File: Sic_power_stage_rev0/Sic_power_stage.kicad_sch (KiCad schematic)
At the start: 39 parts, among them J1 20021321-00006C4LF, J2 20021321-00006C4LF, J3 20021321-00006C4LF, J4 20021321-00006C4LF, J5 20021321-00006C4LF, J6 20021321-00006C4LF, J7 20021321-00006C4LF, J8 20021321-00006C4LF

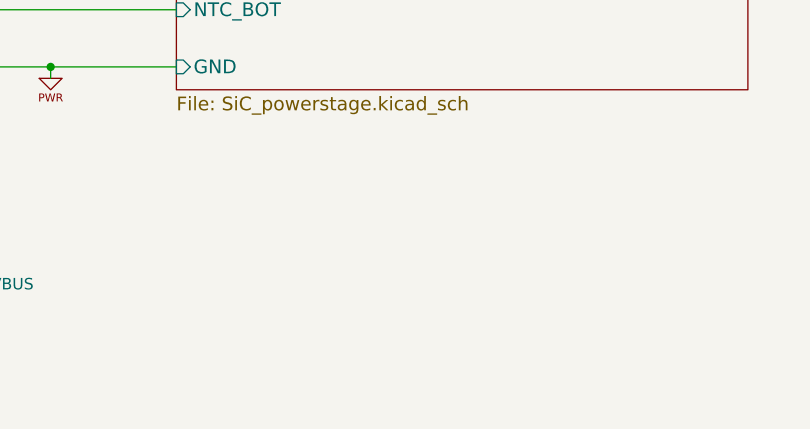
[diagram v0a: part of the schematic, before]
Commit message: WIP: define custom rules, change inner layer PWRGND , VBUS
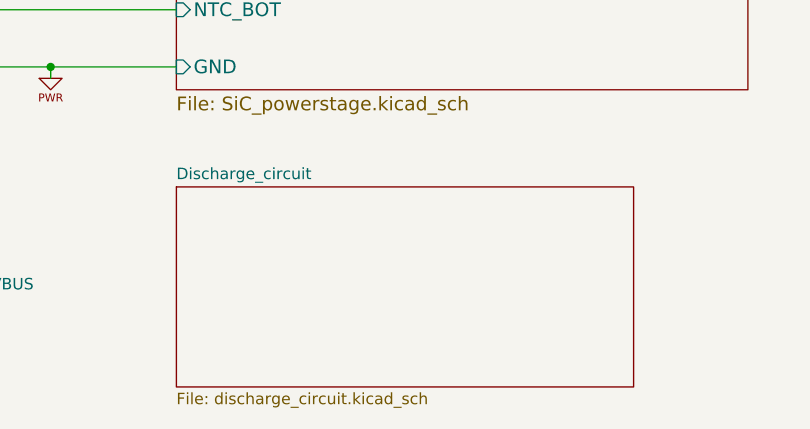
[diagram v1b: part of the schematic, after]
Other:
- added sheet Discharge_circuit (discharge_circuit.kicad_sch)
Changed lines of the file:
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@@
+	)
+	(sheet
+		(at 119.38 170.815)
+		(size 50.8 22.225)
+		(fields_autoplaced yes)
+		(stroke
+			(width 0.1524)
+			(type solid)
+		)
+		(fill
+			(color 0 0 0 0.0000)
+		)
+		(property "Sheetname" "Discharge_circuit"
+			(at 119.38 170.1034 0)
+			(effects
+				(font
+					(size 1.27 1.27)
+				)
+				(justify left bottom)
+			)
+		)
+		(property "Sheetfile" "discharge_circuit.kicad_sch"
+			(at 119.38 193.6246 0)
+			(effects
+				(font
+					(size 1.27 1.27)
+				)
+				(justify left top)
+			)
+		)
+		(instances
+			(project "Sic_power_stage"
+				(path "/40c6bde6-dca0-40b2-8abd-1f20772cb34b"
+					(page "5")
+				)
+			)
+		)
 	)
 	(sheet

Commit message: Increase clearance between mosfets, Add alternating film capacitor
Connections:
- net nc: now reaches J2.1
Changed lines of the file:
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@@
 	)
 	(no_connect
-		(at 100.33 55.88)
+		(at 99.06 58.42)
 	)
 	(no_connect
@@
 	(wire
 		(pts
+			(xy 99.06 55.88) (xy 99.06 58.42)
+		)
+		(stroke
+			(width 0)
+			(type default)
+		)
+	)
+	(wire
+		(pts
 			(xy 110.49 132.08) (xy 119.38 132.08)
 		)
@@
 			(type default)
 			(color 0 0 255 1)
+		)
+	)
+	(wire
+		(pts
+			(xy 100.33 55.88) (xy 99.06 55.88)
+		)
+		(stroke
+			(width 0)
+			(type default)
 		)
 	)
@@
 			)
 			(justify left bottom)
+		)
+	)
+	(label "nc"
+		(at 99.06 55.88 0)
+		(fields_autoplaced yes)
+		(effects
+			(font
+				(size 1.27 1.27)
+			)
+			(justify left bottom)

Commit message: Define Ceralink capacitor value and qty
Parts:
- renumbered J7 to J1, J8 to J2, J1 to J3, J2 to J4, J3 to J5, J4 to J6, J5 to J7, J6 to J8, R40 to R1, R41 to R2, R42 to R3, STANDOFF16 to STANDOFF1, STANDOFF5 to STANDOFF10, STANDOFF6 to STANDOFF11, STANDOFF7 to STANDOFF12, STANDOFF8 to STANDOFF13, STANDOFF9 to STANDOFF14, STANDOFF10 to STANDOFF15, STANDOFF11 to STANDOFF16, STANDOFF12 to STANDOFF17, STANDOFF13 to STANDOFF18, STANDOFF14 to STANDOFF19, STANDOFF17 to STANDOFF2, STANDOFF15 to STANDOFF20, STANDOFF18 to STANDOFF3, STANDOFF19 to STANDOFF4, STANDOFF20 to STANDOFF5, STANDOFF1 to STANDOFF6, STANDOFF2 to STANDOFF7, STANDOFF3 to STANDOFF8, STANDOFF4 to STANDOFF9

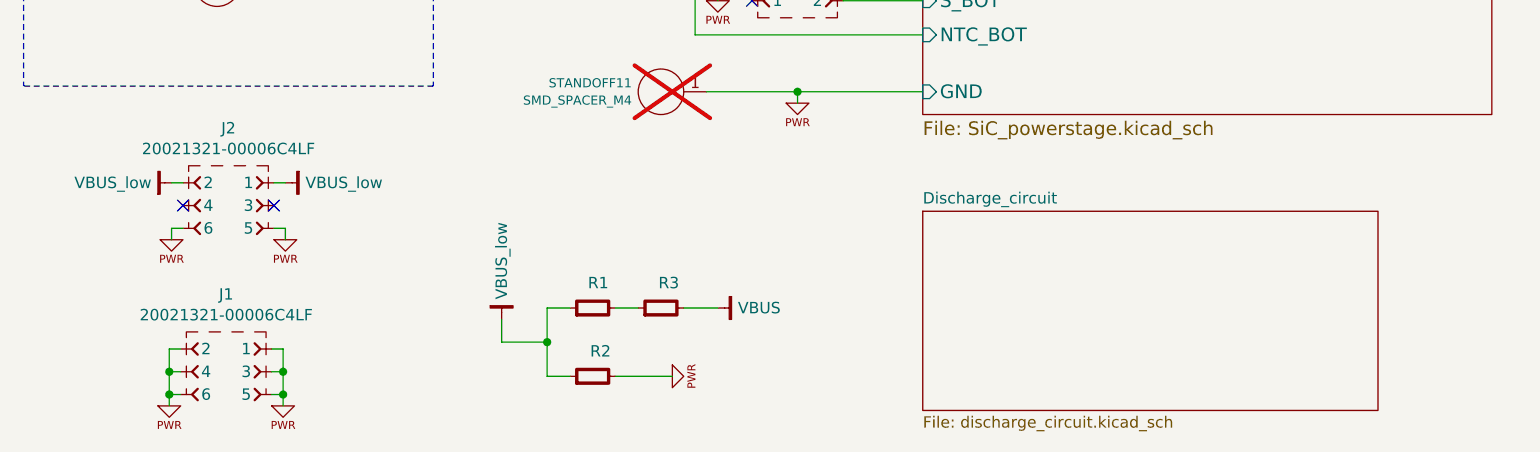
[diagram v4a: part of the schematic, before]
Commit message: Add changes
 - Add DC-LINK capacitor discharge circuit.
 - VBUS resistive divider.
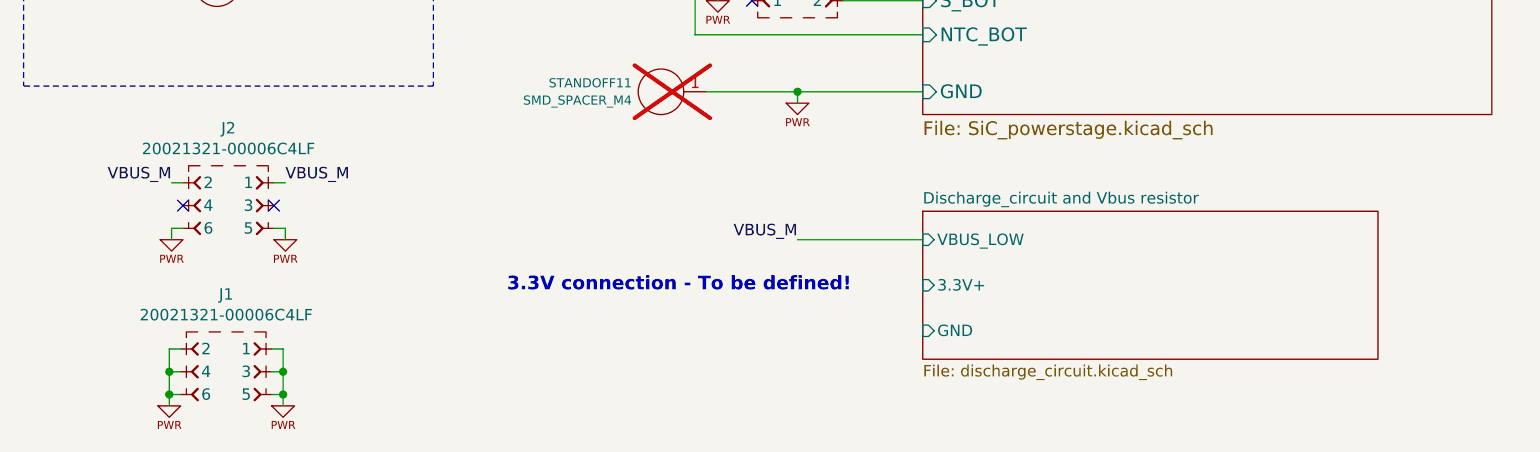
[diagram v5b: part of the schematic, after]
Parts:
- removed R1, R2, R3: R-1206, IPC7351-Nominal:RESC3216X60, symbol pasv-res:R-1206
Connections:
- net VBUS_low renamed VBUS_M
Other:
- sheet Discharge_circuit renamed Discharge_circuit and Vbus resistor
- sheet Discharge_circuit and Vbus resistor ports: added 3.3V+, GND, VBUS_LOW; removed none
- note added: "3.3V connection - To be defined!"

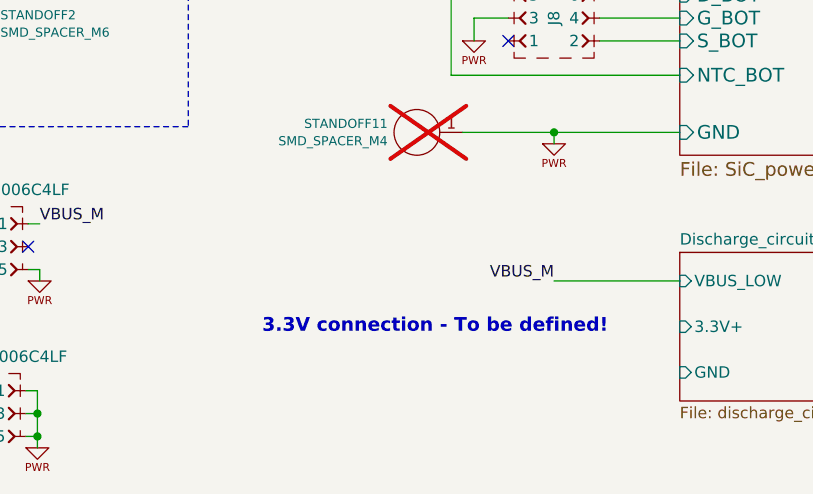
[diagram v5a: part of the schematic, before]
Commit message: SiC: define routing for leg C
Signed-off-by: Ayarde Christian <cayarde@paltatech.com>
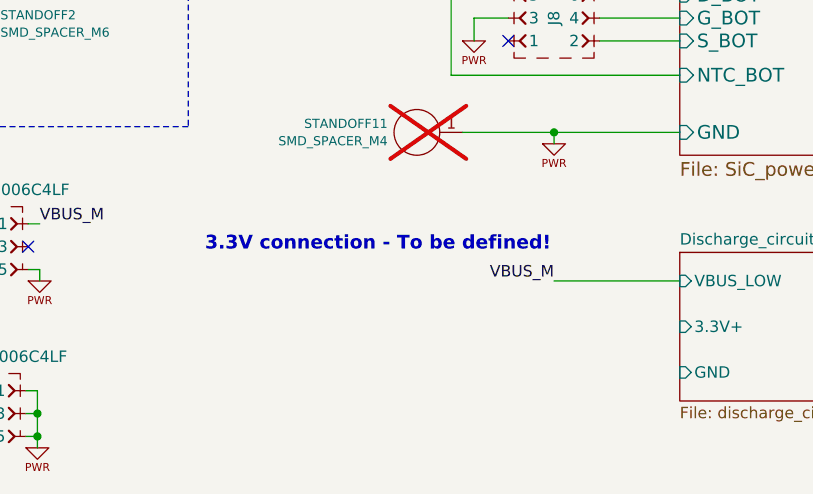
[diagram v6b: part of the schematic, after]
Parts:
- J1, J2, J3, J4, J5, J6, J7, J8: footprint conn-fci:CONN-20021321-00006C4LF -> conn-fci:CONN-20021321-00006C4LF-no-hole
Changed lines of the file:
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@@
 	(text "3.3V connection - To be defined!"
 		(exclude_from_sim no)
-		(at 92.202 179.07 0)
+		(at 85.852 169.926 0)
 		(effects
 			(font
@@
 			)
 		)
-		(property "Footprint" "conn-fci:CONN-20021321-00006C4LF"
+		(property "Footprint" "conn-fci:CONN-20021321-00006C4LF-no-hole"
 			(at 105.41 127 0)
 			(effects
@@
 			)
 		)
-		(property "Footprint" "conn-fci:CONN-20021321-00006C4LF"
+		(property "Footprint" "conn-fci:CONN-20021321-00006C4LF-no-hole"
 			(at 41.656 186.182 0)
 			(effects
@@
 			)
 		)
-		(property "Footprint" "conn-fci:CONN-20021321-00006C4LF"
+		(property "Footprint" "conn-fci:CONN-20021321-00006C4LF-no-hole"
 			(at 41.91 167.64 0)
 			(effects
@@
 			)
 		)
-		(property "Footprint" "conn-fci:CONN-20021321-00006C4LF"
+		(property "Footprint" "conn-fci:CONN-20021321-00006C4LF-no-hole"
 			(at 105.41 55.88 0)
 			(effects
@@
 			)
 		)
-		(property "Footprint" "conn-fci:CONN-20021321-00006C4LF"
+		(property "Footprint" "conn-fci:CONN-20021321-00006C4LF-no-hole"
 			(at 105.41 101.6 0)
 			(effects
@@
 			)
 		)
-		(property "Footprint" "conn-fci:CONN-20021321-00006C4LF"
+		(property "Footprint" "conn-fci:CONN-20021321-00006C4LF-no-hole"
 			(at 105.41 35.56 0)
 			(effects
@@
 			)
 		)
-		(property "Footprint" "conn-fci:CONN-20021321-00006C4LF"
+		(property "Footprint" "conn-fci:CONN-20021321-00006C4LF-no-hole"
 			(at 105.41 81.28 0)
 			(effects
@@
 			)
 		)
-		(property "Footprint" "conn-fci:CONN-20021321-00006C4LF"
+		(property "Footprint" "conn-fci:CONN-20021321-00006C4LF-no-hole"
 			(at 105.41 147.32 0)
 			(effects

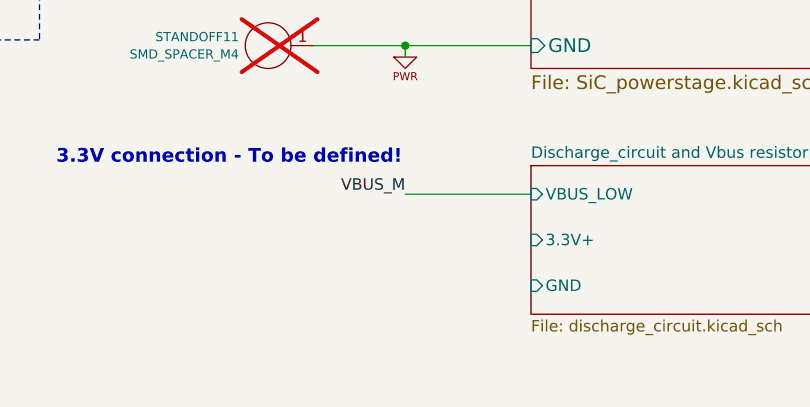
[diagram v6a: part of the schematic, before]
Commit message: SiC: Change DC-LINK MLCC capacitor
 - Originally, the estimation about the ceramic capacitor value was 0.25uF. This is for CERALINK capacitor as the DC-BIAS
   affects its capacitance just 1% for 400V. Now a MLCC was chosen, and the DC-BIAS is into account for this application
   would be great to test with both capacitors and check the bahaviour between them.

Signed-off-by: Ayarde Christian <cayarde@paltatech.com>
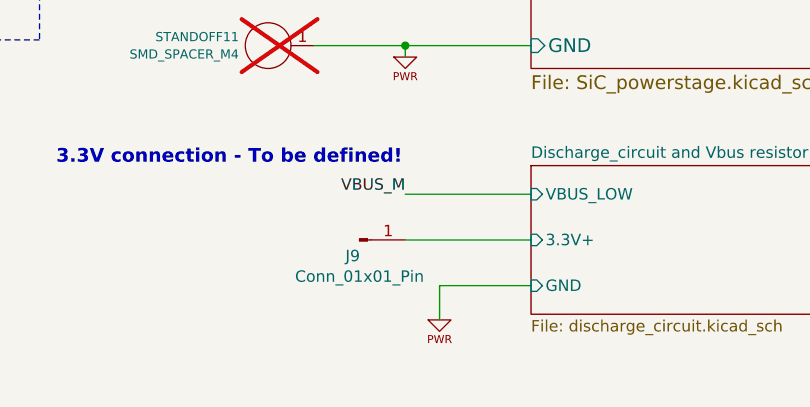
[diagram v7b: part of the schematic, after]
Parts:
- added J9: Conn_01x01_Pin, Connector_PinHeader_1.00mm:PinHeader_1x01_P1.00mm_Vertical, symbol Connector:Conn_01x01_Pin
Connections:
- net Discharge_circuit and Vbus resistor/3.3V+: now also J9.1 (Pin_1)
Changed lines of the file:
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@@
 	(wire
 		(pts
+			(xy 109.22 187.96) (xy 109.22 184.15)
+		)
+		(stroke
+			(width 0)
+			(type default)
+		)
+	)
+	(wire
+		(pts
 			(xy 36.576 188.722) (xy 35.306 188.722)
 		)
@@
 	(wire
 		(pts
+			(xy 109.22 184.15) (xy 119.38 184.15)
+		)
+		(stroke
+			(width 0)
+			(type default)
+		)
+	)
+	(wire
+		(pts
 			(xy 35.306 192.532) (xy 35.306 191.262)
 		)
@@
 	(wire
 		(pts
+			(xy 105.41 179.07) (xy 119.38 179.07)
+		)
+		(stroke
+			(width 0)
+			(type default)
+		)
+	)
+	(wire
+		(pts
 			(xy 95.25 157.48) (xy 105.41 157.48)
 		)
@@
 	)
 	(symbol
+		(lib_id "power1:PWRGND")
+		(at 109.22 187.96 0)
+		(unit 1)
+		(exclude_from_sim no)
+		(in_bom yes)
+		(on_board yes)
+		(dnp no)
+		(property "Reference" "#PWR010"
+			(at 109.22 187.96 0)
+			(effects
+				(font
+					(size 0.762 0.762)
+				)
+				(hide yes)
+			)
+		)
+		(property "Value" "PWRGND"
+			(at 109.22 189.738 0)
+			(effects
+				(font
+					(size 0.762 0.762)
+				)
+				(hide yes)
+			)
+		)
+		(property "Footprint" ""
+			(at 109.22 187.96 0)
+			(effects
+				(font
+					(size 1.524 1.524)
+				)
+			)
+		)
+		(property "Datasheet" ""
+			(at 109.22 187.96 0)
+			(effects
+				(font
+					(size 1.524 1.524)
+				)
+			)
+		)
+		(property "Description" ""
+			(at 109.22 187.96 0)
+			(effects
+				(font
+					(size 1.27 1.27)
+				)
+				(hide yes)
+			)
+		)
+		(pin "1"
+		)
+		(instances
+			(project "Sic_power_stage"
+				(path "/40c6bde6-dca0-40b2-8abd-1f20772cb34b"
+					(reference "#PWR010")
+					(unit 1)
+				)
+			)
+		)
+	)
+	(symbol
 		(lib_id "conn-100mil:CONN-100MIL-F-2x3")
 		(at 105.41 35.56 0)
@@
 					(unit 1)
 				)
+			)
+		)
+	)
+	(symbol
+		(lib_id "Connector:Conn_01x01_Pin")
+		(at 100.33 179.07 0)
+		(unit 1)
+		(exclude_from_sim no)
+		(in_bom yes)
+		(on_board yes)
+		(dnp no)
+		(property "Reference" "J9"
+			(at 99.568 180.848 0)
+			(effects
+				(font
+					(size 1.27 1.27)
+				)
+			)
+		)
+		(property "Value" "Conn_01x01_Pin"
+			(at 100.33 183.134 0)
+			(effects
+				(font
+					(size 1.27 1.27)
+				)
+			)
+		)
+		(property "Footprint" "Connector_PinHeader_1.00mm:PinHeader_1x01_P1.00mm_Vertical"
+			(at 100.33 179.07 0)
+			(effects
+				(font
+					(size 1.27 1.27)
+				)
+				(hide yes)
+			)
+		)
+		(property "Datasheet" "~"
+			(at 100.33 179.07 0)
+			(effects
+				(font
+					(size 1.27 1.27)
+				)
+				(hide yes)
+			)
+		)
+		(property "Description" "Generic connector, single row, 01x01, script generated"
+			(at 100.33 179.07 0)
+			(effects
+				(font
+					(size 1.27 1.27)
+				)
+				(hide yes)
+			)
+		)
+		(pin "1"
+		)
+		(instances
+			(project ""
+				(path "/40c6bde6-dca0-40b2-8abd-1f20772cb34b"
+					(reference "J9")
+					(unit 1)
+				)
